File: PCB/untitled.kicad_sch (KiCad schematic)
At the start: 1 part, among them U2 ICM-20602

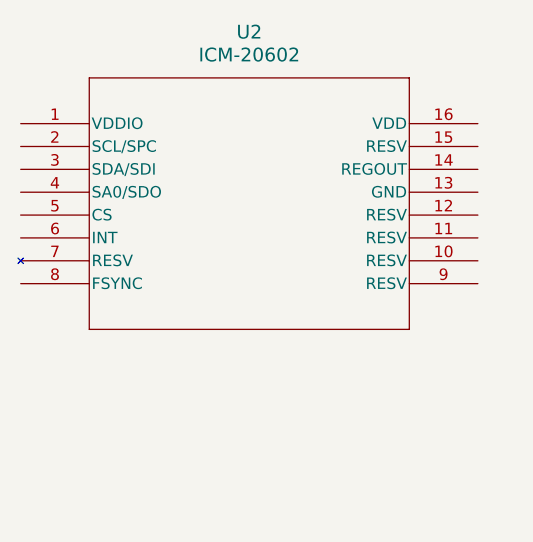
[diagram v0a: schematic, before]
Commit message: New IMU symbol/footprint
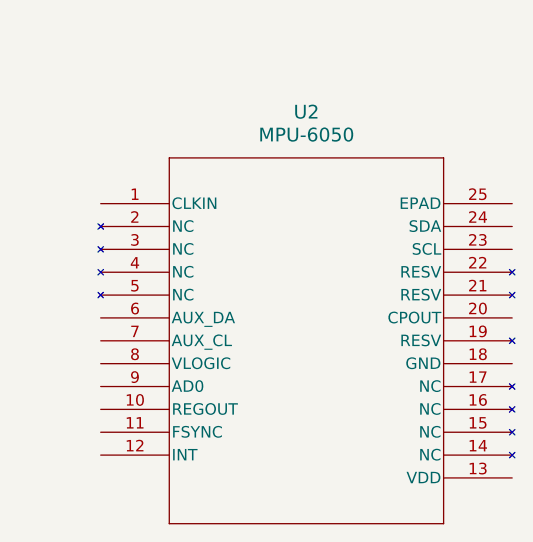
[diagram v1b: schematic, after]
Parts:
- removed U2: ICM-20602, IMU:LGA16_I62_IVS-L, symbol IMU:ICM-20602
- added U2: MPU-6050, IMU:QFN24_4X4X0P9-0P5_TDK-L, symbol IMU:MPU-6050
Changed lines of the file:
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@@
 	(paper "A4")
 	(symbol
-		(lib_id "IMU:ICM-20602")
-		(at 35.56 31.75 0)
+		(lib_id "IMU:MPU-6050")
+		(at 44.45 40.64 0)
 		(unit 1)
 		(exclude_from_sim no)
@@
 		(fields_autoplaced yes)
 		(property "Reference" "U2"
-			(at 60.96 21.59 0)
+			(at 67.31 30.48 0)
 			(effects
 				(font
@@
 			)
 		)
-		(property "Value" "ICM-20602"
-			(at 60.96 24.13 0)
+		(property "Value" "MPU-6050"
+			(at 67.31 33.02 0)
 			(effects
 				(font
@@
 			)
 		)
-		(property "Footprint" "IMU:LGA16_I62_IVS-L"
-			(at 35.56 31.75 0)
+		(property "Footprint" "IMU:QFN24_4X4X0P9-0P5_TDK-L"
+			(at 44.45 40.64 0)
 			(effects
 				(font
@@
 			)
 		)
-		(property "Datasheet" "ICM-20602"
-			(at 35.56 31.75 0)
+		(property "Datasheet" "MPU-6050"
+			(at 44.45 40.64 0)
 			(effects
 				(font
@@
 		)
 		(property "Description" ""
-			(at 35.56 31.75 0)
+			(at 44.45 40.64 0)
 			(effects
 				(font
@@
 			)
 		)
+		(pin "9"
+		)
+		(pin "4"
+		)
+		(pin "24"
+		)
+		(pin "22"
+		)
+		(pin "20"
+		)
+		(pin "1"
+		)
+		(pin "3"
+		)
+		(pin "6"
+		)
+		(pin "2"
+		)
 		(pin "5"
 		)
 		(pin "7"
 		)
-		(pin "1"
+		(pin "8"
 		)
-		(pin "4"
+		(pin "10"
 		)
-		(pin "6"
+		(pin "11"
 		)
-		(pin "3"
+		(pin "12"
 		)
-		(pin "9"
+		(pin "25"
 		)
-		(pin "2"
+		(pin "23"
+		)
+		(pin "21"
+		)
+		(pin "19"
+		)
+		(pin "18"
 		)
 		(pin "16"
@@
 		(pin "15"
 		)
-		(pin "11"
-		)
-		(pin "12"
-		)
-		(pin "8"
-		)
 		(pin "14"
-		)
-		(pin "10"
 		)
 		(pin "13"
 		)
+		(pin "17"
+		)
 		(instances
 			(project ""
+				(path "/28141696-683e-41f2-9aa1-d13841c0e19e"
+					(reference "U1")
+					(unit 1)
+				)
+			)
+			(project "Smart_Backpack"
 				(path "/38abc652-c887-4ef7-a45f-d93ca7f4b2d6/d6ce3c21-a733-4fa1-8134-cea10a02c4e5"
 					(reference "U2")
@@
 		)
 	)
+	(sheet_instances
+		(path "/"
+			(page "1")
+		)
+	)
+	(embedded_fonts no)
 )

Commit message: work on IMU
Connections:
- no-connect marks 0 -> 5
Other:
- moved on the sheet: U2
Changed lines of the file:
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@@
 	(generator_version "9.0")
 	(paper "A4")
+	(no_connect
+		(at 143.51 78.74)
+	)
+	(no_connect
+		(at 143.51 93.98)
+	)
+	(no_connect
+		(at 143.51 104.14)
+	)
+	(no_connect
+		(at 143.51 91.44)
+	)
+	(no_connect
+		(at 143.51 99.06)
+	)
 	(symbol
 		(lib_id "IMU:MPU-6050")
-		(at 44.45 40.64 0)
+		(at 143.51 78.74 0)
 		(unit 1)
 		(exclude_from_sim no)
@@
 		(fields_autoplaced yes)
 		(property "Reference" "U2"
-			(at 67.31 30.48 0)
+			(at 166.37 68.58 0)
 			(effects
 				(font
@@
 		)
 		(property "Value" "MPU-6050"
-			(at 67.31 33.02 0)
+			(at 166.37 71.12 0)
 			(effects
 				(font
@@
 		)
 		(property "Footprint" "IMU:QFN24_4X4X0P9-0P5_TDK-L"
-			(at 44.45 40.64 0)
+			(at 143.51 78.74 0)
 			(effects
 				(font
@@
 		)
 		(property "Datasheet" "MPU-6050"
-			(at 44.45 40.64 0)
+			(at 143.51 78.74 0)
 			(effects
 				(font
@@
 		)
 		(property "Description" ""
-			(at 44.45 40.64 0)
+			(at 143.51 78.74 0)
 			(effects
 				(font

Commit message: IMU done yay
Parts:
- added C4: 2.2nF, symbol Device:C
- added C5: 0.1uF, symbol Device:C
- added R4, R5: 10kΩ, symbol Device:R_US
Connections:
- net at U2.10 (REGOUT): now also C5.1
- net IMU_INT: now reaches U2.12 (INT)
- net Buck_3v3: now reaches U2.13 (VDD)
- net Buck_3v3: now also U2.8 (VLOGIC), R4.1, R5.1
- net GND: now reaches U2.18 (GND)
- net GND: now also U2.25 (EPAD), C4.2, C5.2
- net at U2.20 (CPOUT): now also C4.1
- net ESP_SCL: now reaches U2.23 (SCL)
- net ESP_SCL: now also R5.2
- net ESP_SDA: now reaches U2.24 (SDA)
- net ESP_SDA: now also R4.2
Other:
- note added: "IMU Chip"
- note added: "IMU I2C Pullup"
- moved on the sheet: U2

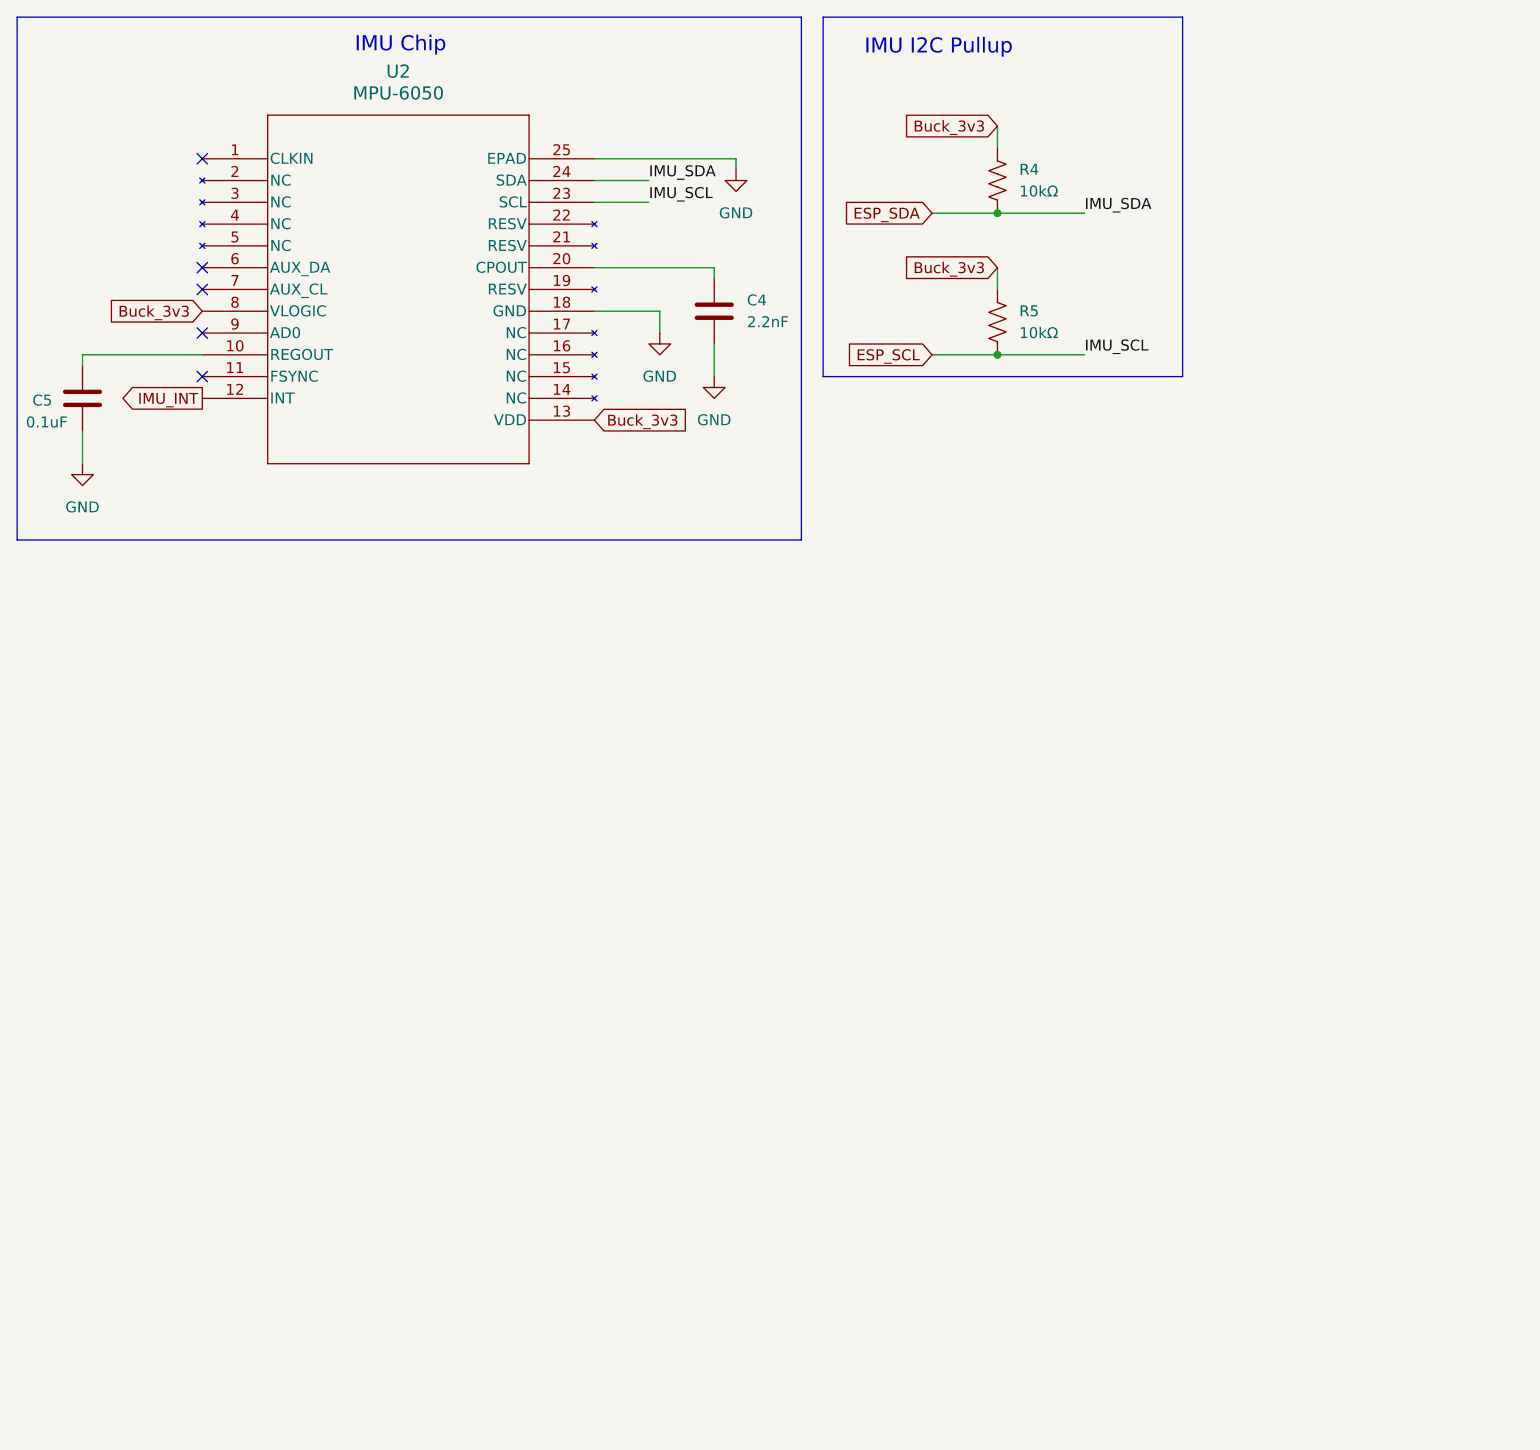
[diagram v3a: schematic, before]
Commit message: add connectors for off-board components
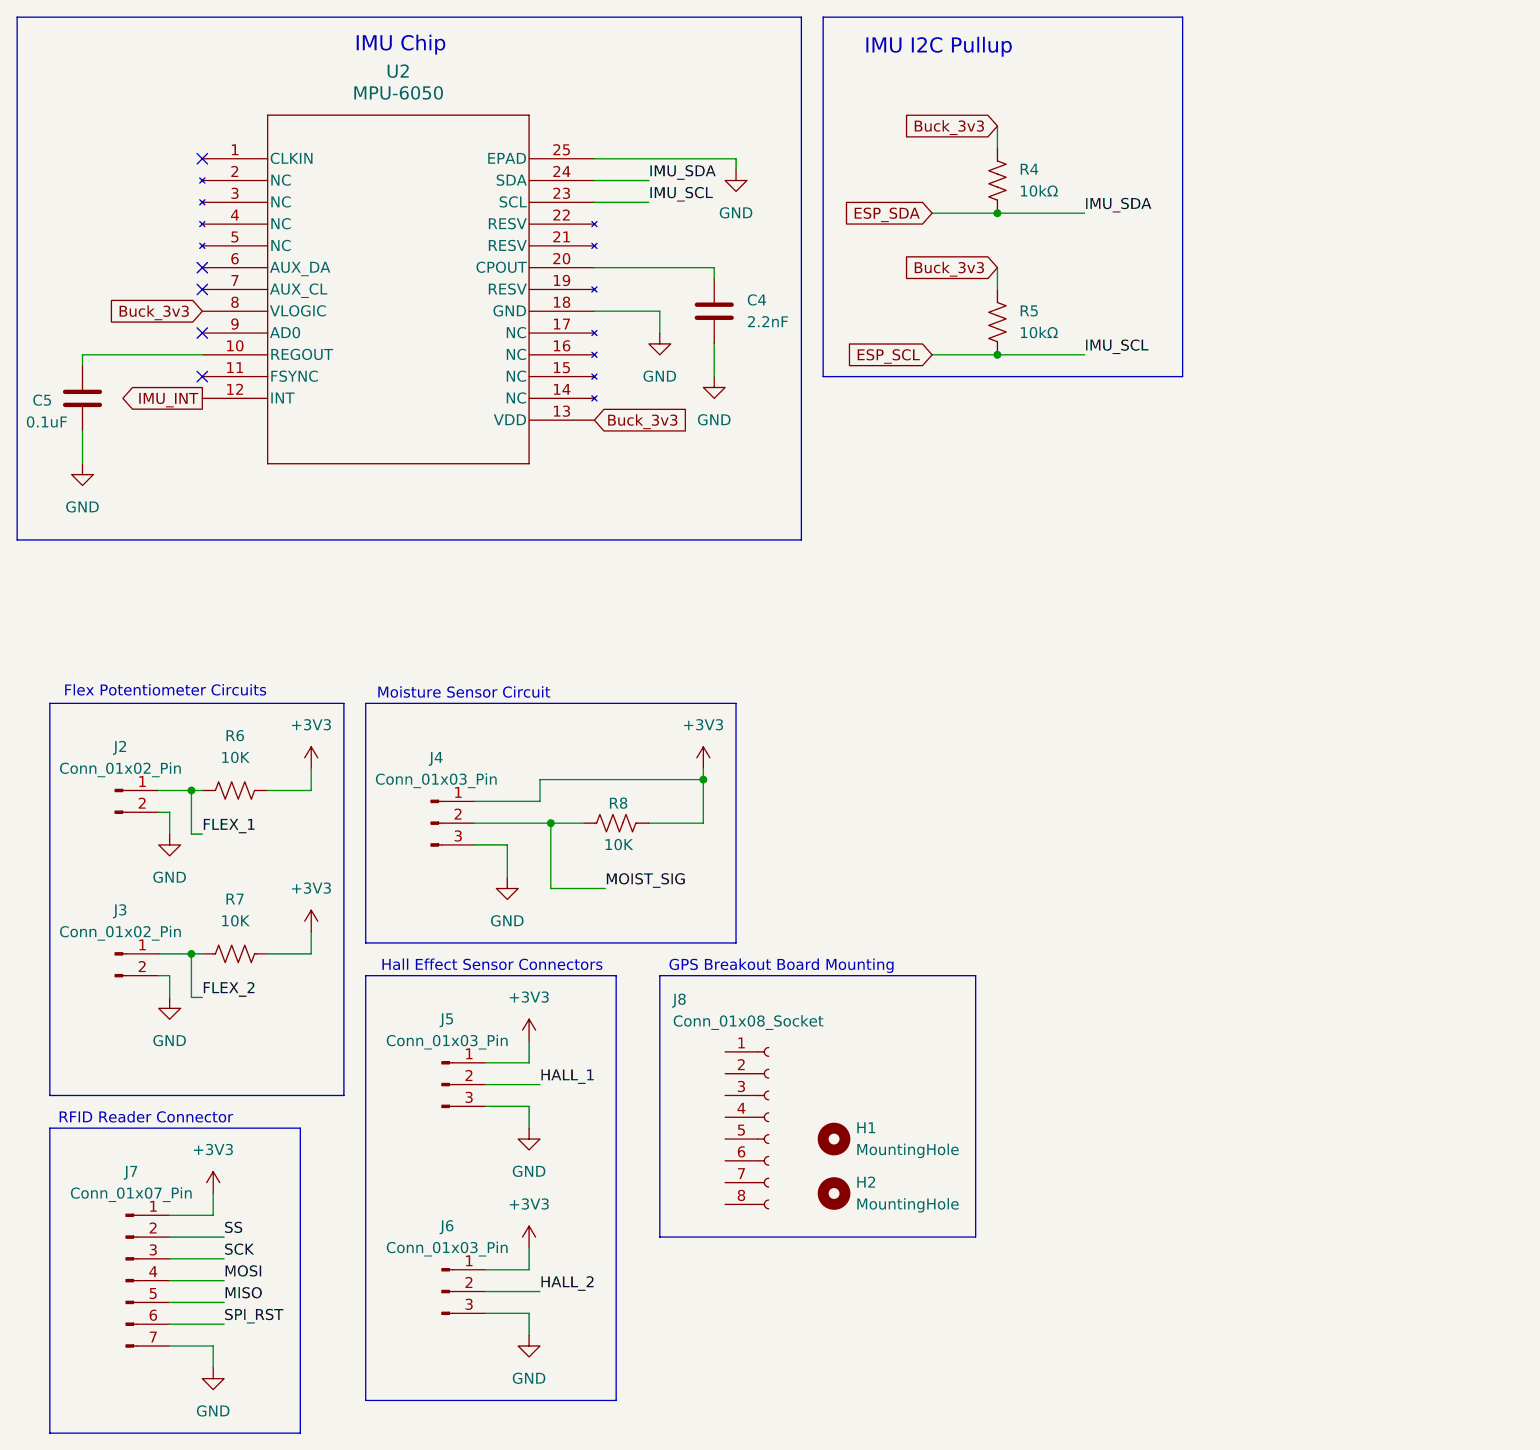
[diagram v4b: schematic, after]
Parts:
- added H1, H2: MountingHole, MountingHole:MountingHole_2.2mm_M2, symbol Mechanical:MountingHole
- added J2, J3: Conn_01x02_Pin, Connector_JST:JST_VH_B2P-VH_1x02_P3.96mm_Vertical, symbol Connector:Conn_01x02_Pin
- added J4, J5, J6: Conn_01x03_Pin, Connector_JST:JST_VH_B3P-VH_1x03_P3.96mm_Vertical, symbol Connector:Conn_01x03_Pin
- added J7: Conn_01x07_Pin, Connector_JST:JST_VH_B7P-VH_1x07_P3.96mm_Vertical, symbol Connector:Conn_01x07_Pin
- added J8: Conn_01x08_Socket, Connector_PinHeader_2.54mm:PinHeader_1x08_P2.54mm_Vertical, symbol Connector:Conn_01x08_Socket
- added R6, R7, R8: 10K, symbol Device:R_US
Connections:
- net GND: now also J2.2 (Pin_2), J3.2 (Pin_2), J4.3 (Pin_3), J5.3 (Pin_3), J6.3 (Pin_3), J7.7 (Pin_7)
- new net +3V3: J4.1 (Pin_1), J5.1 (Pin_1), J6.1 (Pin_1), J7.1 (Pin_1), R6.2, R7.2, R8.2
- new net FLEX_1: J2.1 (Pin_1), R6.1
- new net FLEX_2: J3.1 (Pin_1), R7.1
- new net HALL_1: J5.2 (Pin_2)
- new net HALL_2: J6.2 (Pin_2)
- new net MISO: J7.5 (Pin_5)
- new net MOIST_SIG: J4.2 (Pin_2), R8.1
- new net MOSI: J7.4 (Pin_4)
- new net SCK: J7.3 (Pin_3)
- new net SPI_RST: J7.6 (Pin_6)
- new net SS: J7.2 (Pin_2)
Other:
- note added: "Flex Potentiometer Circuits"
- note added: "GPS Breakout Board Mounting"
- note added: "Hall Effect Sensor Connectors"
- note added: "Moisture Sensor Circuit"
- note added: "RFID Reader Connector"

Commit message: She buck on my converter till I 3.3V DC
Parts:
- added C6: 10uF, symbol Device:C
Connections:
- net Buck_3v3: now also C6.1
- net GND: now also C6.2
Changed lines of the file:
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@@
+	)
+	(junction
+		(at 86.36 60.96)
+		(diameter 0)
+		(color 0 0 0 0)
 	)
 	(junction
@@
 	(wire
 		(pts
+			(xy 86.36 60.96) (xy 86.36 62.23)
+		)
+		(stroke
+			(width 0)
+			(type default)
+		)
+	)
+	(wire
+		(pts
 			(xy 31.75 153.67) (xy 36.83 153.67)
 		)
@@
 	(wire
 		(pts
+			(xy 87.63 60.96) (xy 86.36 60.96)
+		)
+		(stroke
+			(width 0)
+			(type default)
+		)
+	)
+	(wire
+		(pts
 			(xy 21.59 62.23) (xy 21.59 66.04)
 		)
@@
 	(wire
 		(pts
+			(xy 86.36 69.85) (xy 86.36 71.12)
+		)
+		(stroke
+			(width 0)
+			(type default)
+		)
+	)
+	(wire
+		(pts
 			(xy 76.2 107.95) (xy 76.2 115.57)
 		)
@@
 	(wire
 		(pts
-			(xy 95.25 52.07) (xy 95.25 55.88)
+			(xy 95.25 52.07) (xy 95.25 53.34)
+		)
+		(stroke
+			(width 0)
+			(type default)
+		)
+	)
+	(wire
+		(pts
+			(xy 86.36 60.96) (xy 81.28 60.96)
 		)
 		(stroke
@@
 	(global_label "Buck_3v3"
 		(shape input)
-		(at 81.28 60.96 0)
+		(at 87.63 60.96 0)
 		(fields_autoplaced yes)
 		(effects
@@
 		)
 		(property "Intersheetrefs" "${INTERSHEET_REFS}"
-			(at 93.1551 60.96 0)
+			(at 99.5051 60.96 0)
 			(effects
 				(font
@@
 	(symbol
 		(lib_id "power:GND")
-		(at 95.25 55.88 0)
+		(at 95.25 53.34 0)
 		(unit 1)
 		(exclude_from_sim no)
@@
 		(fields_autoplaced yes)
 		(property "Reference" "#PWR09"
-			(at 95.25 62.23 0)
+			(at 95.25 59.69 0)
 			(effects
 				(font
@@
 		)
 		(property "Value" "GND"
-			(at 95.25 60.96 0)
+			(at 95.25 58.42 0)
 			(effects
 				(font
@@
 		)
 		(property "Footprint" ""
-			(at 95.25 55.88 0)
+			(at 95.25 53.34 0)
 			(effects
 				(font
@@
 		)
 		(property "Datasheet" ""
-			(at 95.25 55.88 0)
+			(at 95.25 53.34 0)
 			(effects
 				(font
@@
 		)
 		(property "Description" "Power symbol creates a global label with name \"GND\" , ground"
-			(at 95.25 55.88 0)
+			(at 95.25 53.34 0)
 			(effects
 				(font
@@
 	)
 	(symbol
+		(lib_id "Device:C")
+		(at 86.36 66.04 0)
+		(unit 1)
+		(exclude_from_sim no)
+		(in_bom yes)
+		(on_board yes)
+		(dnp no)
+		(fields_autoplaced yes)
+		(property "Reference" "C6"
+			(at 90.17 64.7699 0)
+			(effects
+				(font
+					(size 1.27 1.27)
+				)
+				(justify left)
+			)
+		)
+		(property "Value" "10uF"
+			(at 90.17 67.3099 0)
+			(effects
+				(font
+					(size 1.27 1.27)
+				)
+				(justify left)
+			)
+		)
+		(property "Footprint" ""
+			(at 87.3252 69.85 0)
+			(effects
+				(font
+					(size 1.27 1.27)
+				)
+				(hide yes)
+			)
+		)
+		(property "Datasheet" "~"
+			(at 86.36 66.04 0)
+			(effects
+				(font
+					(size 1.27 1.27)
+				)
+				(hide yes)
+			)
+		)
+		(property "Description" "Unpolarized capacitor"
+			(at 86.36 66.04 0)
+			(effects
+				(font
+					(size 1.27 1.27)
+				)
+				(hide yes)
+			)
+		)
+		(pin "1"
+		)
+		(pin "2"
+		)
+		(instances
+			(project "Smart_Backpack"
+				(path "/38abc652-c887-4ef7-a45f-d93ca7f4b2d6/d6ce3c21-a733-4fa1-8134-cea10a02c4e5"
+					(reference "C6")
+					(unit 1)
+				)
+			)
+		)
+	)
+	(symbol
 		(lib_id "power:+3V3")
 		(at 48.26 120.65 0)
@@
 					(unit 1)
 				)
+			)
+		)
+	)
+	(symbol
+		(lib_id "power:GND")
+		(at 86.36 71.12 0)
+		(unit 1)
+		(exclude_from_sim no)
+		(in_bom yes)
+		(on_board yes)
+		(dnp no)
+		(property "Reference" "#PWR024"
+			(at 86.36 77.47 0)
+			(effects
+				(font
+					(size 1.27 1.27)
+				)
+				(hide yes)
+			)
+		)
+		(property "Value" "GND"
+			(at 89.662 73.152 0)
+			(effects
+				(font
+					(size 1.27 1.27)
+				)
+			)
+		)
+		(property "Footprint" ""
+			(at 86.36 71.12 0)
+			(effects
+				(font
+					(size 1.27 1.27)
+				)
+				(hide yes)
+			)
+		)
+		(property "Datasheet" ""
+			(at 86.36 71.12 0)
+			(effects
+				(font
+					(size 1.27 1.27)
+				)
+				(hide yes)
+			)
+		)
+		(property "Description" "Power symbol creates a global label with name \"GND\" , ground"
+			(at 86.36 71.12 0)
+			(effects
+				(font
+					(size 1.27 1.27)
+				)
+				(hide yes)
+			)
+		)
+		(pin "1"
+		)
+		(instances
+			(project "Smart_Backpack"
+				(path "/38abc652-c887-4ef7-a45f-d93ca7f4b2d6/d6ce3c21-a733-4fa1-8134-cea10a02c4e5"
+					(reference "#PWR024")
+					(unit 1)
+				)
